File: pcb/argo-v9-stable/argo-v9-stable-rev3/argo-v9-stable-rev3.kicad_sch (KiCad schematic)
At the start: 101 parts, among them IC1 MP2672GD, J1 Sparkfun_NEO-N9M-SMA, J2 USB4125-GF-A, J3 LED_power_button_RGB_LED, J4 Conn_I2C_Molex_705450003, J5 Conn_I2C_Molex_705450003, K1 PRL3-5V-DC-1A, Q1 BSD840N, Q2 BSD840N, SW1 POW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

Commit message: **** Argo PCB rev3 sent for JLCPCB fabrication - 3d models for GPS and LORA daughterboards - improved cable connections and i2c headers - many circuit fixes to fix problems with rev2 PCB - improved overvoltage diode protection for FETs and OPi pins - fixed i2c buffer connections - improved power routing - adjusted many R values to be correct - fixed LORA pins and place LORA daughterboard on PCB - moved BNO085 to i2c connector for mounting away from power relay - many additional scope probe test points
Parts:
- added TP7: TestPoint_Probe_autonamed, Argo footprint Library:TestPoint_scope_probe_autonamed, symbol argo-v9:TestPoint_Probe_autonamed
- J1: footprint sparkfun:Sparkfun_NEO-M9N-SMA-scaled -> Argo footprint Library:Sparkfun_NEO-M9N-SMA
- J3: footprint Argo footprint Library:JST_XH_B6B-XH-AM_1x06_P2.50mm_Vertical -> Argo footprint Library:JST_XH_S6B-XH-A_1x06_P2.50mm_Horizontal
- U5: value SHT45-ADB1B -> SHT45
- U7: value TXS0102DCT -> TXS0102; specific part (none) -> TXS0102DCT
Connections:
- net 5V: now also TP7.1
- net POW_BUT: no longer J3.2 (Pin_2), POW_BUT1.2 (A), Q2.2 (G), R25.2, SW1.2, TP6.1
- new net POW_ON: J3.2 (Pin_2), POW_BUT1.2 (A), Q2.2 (G), R25.2, SW1.2, TP6.1
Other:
- note added: "3.3V zener"
- note added: "IMU BNO055 I2C addr 0x69"
- note removed: "Check !CHARGING when OPi running, might need pullup or pulldown"
- note removed: "IMU I2C addr 0x69"
- note removed: "check order!"
- moved on the sheet: D2, D3
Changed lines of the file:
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@@
 		)
 	)
-	(text "check order!"
+	(text "IMU BNO055 I2C addr 0x69"
 		(exclude_from_sim no)
-		(at 327.406 145.542 0)
-		(effects
-			(font
-				(size 1.27 1.27)
-			)
-		)
-	)
-	(text "IMU I2C addr 0x69"
-		(exclude_from_sim no)
-		(at 211.836 82.804 0)
+		(at 216.916 82.804 0)
 		(effects
 			(font
@@
 	(text "Diodes protect FET\ndrains when relay \ncoils turn off and\ncreate voltage\nspike above FUSE=battery"
 		(exclude_from_sim no)
-		(at 193.548 213.36 0)
+		(at 191.516 214.884 0)
 		(effects
 			(font
@@
 		)
 	)
+	(text "3.3V zener"
+		(exclude_from_sim no)
+		(at 214.122 209.296 0)
+		(effects
+			(font
+				(size 0.889 0.889)
+			)
+			(justify right)
+		)
+	)
 	(text "4-wire: 2 green are button,\nred/black are red LED"
 		(exclude_from_sim no)
@@
 	(text "SDP32 I2C 0x21,22,23"
 		(exclude_from_sim no)
-		(at 218.694 102.108 0)
+		(at 217.932 102.616 0)
 		(effects
 			(font
@@
 		)
 	)
-	(text "Check !CHARGING when OPi running, might need pullup or pulldown"
-		(exclude_from_sim no)
-		(at 201.168 131.318 0)
-		(effects
-			(font
-				(size 0.8382 0.8382)
-				(thickness 0.254)
-				(bold yes)
-				(color 255 0 0 1)
-			)
-		)
-	)
 	(junction
 		(at 271.78 114.3)
@@
 	)
 	(junction
-		(at 190.5 198.12)
+		(at 194.31 207.01)
 		(diameter 0)
 		(color 0 0 0 0)
@@
 	)
 	(junction
+		(at 186.69 196.85)
+		(diameter 0)
+		(color 0 0 0 0)
+	)
+	(junction
 		(at 120.65 177.8)
 		(diameter 0)
@@
 	)
 	(junction
-		(at 190.5 208.28)
-		(diameter 0)
-		(color 0 0 0 0)
-	)
-	(junction
 		(at 294.64 139.7)
 		(diameter 0)
@@
 	)
 	(junction
+		(at 176.53 179.07)
+		(diameter 0)
+		(color 0 0 0 0)
+	)
+	(junction
 		(at 224.79 201.93)
 		(diameter 0)
@@
 	(wire
 		(pts
-			(xy 185.42 208.28) (xy 190.5 208.28)
+			(xy 181.61 196.85) (xy 186.69 196.85)
 		)
 		(stroke
@@
 	(wire
 		(pts
-			(xy 224.79 196.85) (xy 224.79 201.93)
-		)
-		(stroke
-			(width 0)
-			(type default)
-		)
-	)
-	(wire
-		(pts
 			(xy 119.38 219.71) (xy 119.38 213.36)
 		)
@@
 	(wire
 		(pts
-			(xy 190.5 196.85) (xy 190.5 198.12)
+			(xy 194.31 209.55) (xy 194.31 207.01)
 		)
 		(stroke
@@
 	(wire
 		(pts
-			(xy 190.5 198.12) (xy 190.5 200.66)
+			(xy 194.31 207.01) (xy 194.31 204.47)
 		)
 		(stroke
@@
 	(wire
 		(pts
-			(xy 198.12 196.85) (xy 198.12 198.12)
+			(xy 186.69 209.55) (xy 186.69 207.01)
 		)
 		(stroke
@@
 	(wire
 		(pts
-			(xy 190.5 208.28) (xy 198.12 208.28)
+			(xy 194.31 196.85) (xy 186.69 196.85)
 		)
 		(stroke
@@
 	)
 	(label "FUSE"
-		(at 185.42 208.28 180)
+		(at 181.61 196.85 0)
 		(effects
 			(font
 				(size 1.27 1.27)
 			)
-			(justify right bottom)
+			(justify left bottom)
 		)
 	)
@@
 	)
 	(label "PSR"
-		(at 198.12 196.85 0)
+		(at 186.69 209.55 180)
 		(effects
 			(font
 				(size 1.27 1.27)
 			)
-			(justify left bottom)
+			(justify right bottom)
 		)
 	)
@@
 	)
 	(label "OFFR"
-		(at 190.5 196.85 180)
+		(at 194.31 209.55 0)
 		(effects
 			(font
 				(size 1.27 1.27)
 			)
-			(justify right bottom)
+			(justify left bottom)
 		)
 	)
@@
 			)
 		)
-		(property "Value" "TXS0102DCT"
+		(property "Value" "TXS0102"
 			(at 130.048 87.376 0)
 			(effects
@@
 			)
 		)
+		(property "specific part" "TXS0102DCT"
+			(at 135.89 82.55 0)
+			(effects
+				(font
+					(size 1.27 1.27)
+				)
+				(hide yes)
+			)
+		)
 		(pin "5"
 		)
@@
 	(symbol
 		(lib_id "argo-v9:TS4148_RCG")
-		(at 198.12 203.2 270)
+		(at 186.69 201.93 90)
 		(unit 1)
 		(exclude_from_sim no)
@@
 		(dnp no)
 		(property "Reference" "D3"
-			(at 195.58 205.74 90)
+			(at 189.23 199.39 90)
 			(effects
 				(font
@@
 		)
 		(property "Value" "TS4148_RCG"
-			(at 194.818 196.596 0)
+			(at 189.992 208.534 0)
 			(effects
 				(font
@@
 		)
 		(property "Footprint" "Argo footprint Library:DIO_TS4148_RCG"
-			(at 198.12 203.2 0)
+			(at 186.69 201.93 0)
 			(effects
 				(font
@@
 		)
 		(property "Datasheet" "https://services.ts.com.tw/storage/resources/datasheet/TS4148%20SERIES_A2301.pdf"
-			(at 198.12 203.2 0)
+			(at 186.69 201.93 0)
 			(effects
 				(font
@@
 		)
 		(property "Description" "100mA - 150mA, 75V Surface Mount Switching Diode"
-			(at 198.12 203.2 0)
+			(at 186.69 201.93 0)
 			(effects
 				(font
@@
 		)
 		(property "PARTREV" "A2301"
-			(at 198.12 203.2 0)
+			(at 186.69 201.93 0)
 			(effects
 				(font
@@
 		)
 		(property "SNAPEDA_PN" "TS4148 RCG"
-			(at 198.12 203.2 0)
+			(at 186.69 201.93 0)
 			(effects
 				(font
@@
 		)
 		(property "MANUFACTURER" "Taiwan Semiconductors"
-			(at 198.12 203.2 0)
+			(at 186.69 201.93 0)
 			(effects
 				(font
@@
 		)
 		(property "MAXIMUM_PACKAGE_HEIGHT" "0.75mm"
-			(at 198.12 203.2 0)
+			(at 186.69 201.93 0)
 			(effects
 				(font
@@
 		)
 		(property "STANDARD" "Manufacturer Recommendations"
-			(at 198.12 203.2 0)
+			(at 186.69 201.93 0)
 			(effects
 				(font
@@
 		)
 		(property "digikey" "https://www.digikey.ch/en/products/detail/taiwan-semiconductor-corporation/TS4148-RCG/7359811"
-			(at 198.12 203.2 0)
+			(at 186.69 201.93 0)
 			(effects
 				(font
@@
 			)
 		)
-		(property "Footprint" "Argo footprint Library:JST_XH_B6B-XH-AM_1x06_P2.50mm_Vertical"
+		(property "Footprint" "Argo footprint Library:JST_XH_S6B-XH-A_1x06_P2.50mm_Horizontal"
 			(at 266.7 172.466 0)
 			(effects
@@
 			)
 		)
-		(property "Footprint" "sparkfun:Sparkfun_NEO-M9N-SMA-scaled"
+		(property "Footprint" "Argo footprint Library:Sparkfun_NEO-M9N-SMA"
 			(at 187.96 59.69 0)
 			(effects
@@
 	)
 	(symbol
+		(lib_id "argo-v9:TestPoint_Probe_autonamed")
+		(at 176.53 179.07 90)
+		(unit 1)
+		(exclude_from_sim no)
+		(in_bom yes)
+		(on_board yes)
+		(dnp no)
+		(fields_autoplaced yes)
+		(property "Reference" "TP7"
+			(at 174.9425 173.99 90)
+			(effects
+				(font
+					(size 1.27 1.27)
+				)
+			)
+		)
+		(property "Value" "TestPoint_Probe_autonamed"
+			(at 172.466 177.419 0)
+			(show_name yes)
+			(effects
+				(font
+					(size 1.27 1.27)
+				)
+				(hide yes)
+			)
+		)
+		(property "Footprint" "Argo footprint Library:TestPoint_scope_probe_autonamed"
+			(at 176.53 173.99 0)
+			(effects
+				(font
+					(size 1.27 1.27)
+				)
+				(hide yes)
+			)
+		)
+		(property "Datasheet" "~"
+			(at 176.53 173.99 0)
+			(effects
+				(font
+					(size 1.27 1.27)
+				)
+				(hide yes)
+			)
+		)
+		(property "Description" "test point (alternative probe-style design)"
+			(at 176.53 179.07 0)
+			(effects
+				(font
+					(size 1.27 1.27)
+				)
+				(hide yes)
+			)
+		)
+		(pin "1"
+		)
+		(instances
+			(project ""
+				(path "/94ef8c18-8f4d-4fb8-af3c-a2b214cf3496"
+					(reference "TP7")
+					(unit 1)
+				)
+			)
+		)
+	)
+	(symbol
 		(lib_id "argo-v9:TS4148_RCG")
-		(at 190.5 203.2 270)
+		(at 194.31 201.93 90)
 		(unit 1)
 		(exclude_from_sim no)
@@
 		(dnp no)
 		(property "Reference" "D2"
-			(at 187.452 205.232 90)
+			(at 197.358 199.898 90)
 			(effects
 				(font
@@
 		)
 		(property "Value" "TS4148_RCG"
-			(at 186.436 196.596 0)
+			(at 198.374 208.534 0)
 			(effects
 				(font
@@
 		)
 		(property "Footprint" "Argo footprint Library:DIO_TS4148_RCG"
-			(at 190.5 203.2 0)
+			(at 194.31 201.93 0)
 			(effects
 				(font
@@
 		)
 		(property "Datasheet" "https://services.ts.com.tw/storage/resources/datasheet/TS4148%20SERIES_A2301.pdf"
-			(at 190.5 203.2 0)
+			(at 194.31 201.93 0)
 			(effects
 				(font
@@
 		)
 		(property "Description" "100mA - 150mA, 75V Surface Mount Switching Diode"
-			(at 190.5 203.2 0)
+			(at 194.31 201.93 0)
 			(effects
 				(font
@@
 		)
 		(property "PARTREV" "A2301"
-			(at 190.5 203.2 0)
+			(at 194.31 201.93 0)
 			(effects
 				(font
@@
 		)
 		(property "SNAPEDA_PN" "TS4148 RCG"
-			(at 190.5 203.2 0)
+			(at 194.31 201.93 0)
 			(effects
 				(font
@@
 		)
 		(property "MANUFACTURER" "Taiwan Semiconductors"
-			(at 190.5 203.2 0)
+			(at 194.31 201.93 0)
 			(effects
 				(font
@@
 		)
 		(property "MAXIMUM_PACKAGE_HEIGHT" "0.75mm"
-			(at 190.5 203.2 0)
+			(at 194.31 201.93 0)
 			(effects
 				(font
@@
 		)
 		(property "STANDARD" "Manufacturer Recommendations"
-			(at 190.5 203.2 0)
+			(at 194.31 201.93 0)
 			(effects
 				(font
@@
 		)
 		(property "digikey" "https://www.digikey.ch/en/products/detail/taiwan-semiconductor-corporation/TS4148-RCG/7359811"
-			(at 190.5 203.2 0)
+			(at 194.31 201.93 0)
 			(effects
 				(font
@@
 			)
 		)
-		(property "Value" "SHT45-ADB1B"
+		(property "Value" "SHT45"
 			(at 242.57 138.4299 0)
 			(effects

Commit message: argo pcb updates after fab to make things better like visible silkscreen and componet imperovmeents
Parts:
- J4, J5: digikey (150um finish) (none) -> https://www.digikey.ch/en/products/detail/molex/0705450003/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; farnell (none) -> https://ch.farnell.com/molex/70545-0003/connector-header-4p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; series (none) -> https://www.molex.com/en-us/products/series-chart/70545
- R26, R27, R28, R29, R30, R31, R32, R7B1: now not fitted
- TP1, TP10, TP11, TP2, TP3, TP4, TP5, TP6, TP7, TP8, TP9: now left out of the parts list
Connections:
- net ISET: now reaches IC1.5 (ISET), R11.2
- net NTC: now reaches IC1.8 (NTC), R13.2, R21.1
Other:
- note added: "!PG configure as PU - signals that CH221K has found a PD cable (power delivery) and negociated the 5V VBUS. But failure also just indicates original USB (non PD) cable."
- note removed: "!PG configure as PU - signals USB power"
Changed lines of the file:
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@@
 		)
 	)
-	(text "!PG configure as PU - signals USB power"
+	(text "!PG configure as PU - signals that CH221K has found \na PD cable (power delivery) and negociated the 5V VBUS.\nBut failure also just indicates original USB (non PD) cable."
 		(exclude_from_sim no)
 		(at 169.418 136.144 0)
 		(effects
 			(font
-				(size 1.016 1.016)
+				(size 0.762 0.762)
 			)
 			(justify left)
@@
 		)
 	)
+	(label "ISET"
+		(at 290.83 110.49 0)
+		(effects
+			(font
+				(size 1.27 1.27)
+			)
+			(justify left bottom)
+		)
+	)
 	(label "BAT_MID"
 		(at 318.77 139.7 0)
@@
 		)
 	)
+	(label "NTC"
+		(at 288.29 118.11 0)
+		(effects
+			(font
+				(size 1.27 1.27)
+			)
+			(justify left bottom)
+		)
+	)
 	(label "!PG"
 		(at 382.27 181.61 0)
@@
 		(in_bom yes)
 		(on_board yes)
-		(dnp no)
+		(dnp yes)
 		(property "Reference" "R30"
 			(at 342.392 116.332 90)
@@
 		(unit 1)
 		(exclude_from_sim no)
-		(in_bom yes)
+		(in_bom no)
 		(on_board yes)
 		(dnp no)
@@
 		(in_bom yes)
 		(on_board yes)
-		(dnp no)
+		(dnp yes)
 		(property "Reference" "R28"
 			(at 113.284 85.852 90)
@@
 		(unit 1)
 		(exclude_from_sim no)
-		(in_bom yes)
+		(in_bom no)
 		(on_board yes)
 		(dnp no)
@@
 			)
 		)
-		(property "Datasheet" "https://www.wch.cn/downloads/file/301.html"
+		(property "Datasheet" "kicad-embed://CH224DS1.PDF"
 			(at 372.11 165.1 0)
 			(effects
@@
 		(in_bom yes)
 		(on_board yes)
-		(dnp no)
+		(dnp yes)
 		(property "Reference" "R29"
 			(at 111.252 76.962 90)
@@
 		(unit 1)
 		(exclude_from_sim no)
-		(in_bom yes)
+		(in_bom no)
 		(on_board yes)
 		(dnp no)
@@
 		(unit 1)
 		(exclude_from_sim no)
-		(in_bom yes)
+		(in_bom no)
 		(on_board yes)
 		(dnp no)
@@
 		(in_bom yes)
 		(on_board yes)
-		(dnp no)
+		(dnp yes)
 		(property "Reference" "R7B1"
 			(at 114.808 180.34 0)
@@
 		(in_bom yes)
 		(on_board yes)
-		(dnp no)
+		(dnp yes)
 		(property "Reference" "R27"
 			(at 105.918 90.678 90)
@@
 			)
 		)
+		(property "series" "https://www.molex.com/en-us/products/series-chart/70545"
+			(at 214.63 74.93 0)
+			(effects
+				(font
+					(size 1.27 1.27)
+				)
+				(hide yes)
+			)
+		)
+		(property "farnell" "https://ch.farnell.com/molex/70545-0003/connector-header-4pos-1row-2-54mm/dp/3221916"
+			(at 214.63 74.93 0)
+			(effects
+				(font
+					(size 1.27 1.27)
+				)
+				(hide yes)
+			)
+		)
+		(property "digikey (150um finish)" "https://www.digikey.ch/en/products/detail/molex/0705450003/455677?s=N4IgjCBcoBw1oDGUBmBDANgZwKYBoQB7KAbRACYAGAZjADYB2EAXQIAcAXKEAZQ4CcAlgDsA5iAC%2BBMAwCc5BCGSR02fEVIhZsgKx0IrEJ258hYyQQC0AFkXLVuAgDdhqTI42QyO6w3ot2LkgQSQkJIA"
+			(at 214.63 74.93 0)
+			(effects
+				(font
+					(size 1.27 1.27)
+				)
+				(hide yes)
+			)
+		)
 		(pin "2"
 		)
@@
 		(unit 1)
 		(exclude_from_sim no)
-		(in_bom yes)
+		(in_bom no)
 		(on_board yes)
 		(dnp no)
@@
 			)
 		)
+		(property "series" "https://www.molex.com/en-us/products/series-chart/70545"
+			(at 214.63 93.98 0)
+			(effects
+				(font
+					(size 1.27 1.27)
+				)
+				(hide yes)
+			)
+		)
+		(property "farnell" "https://ch.farnell.com/molex/70545-0003/connector-header-4pos-1row-2-54mm/dp/3221916"
+			(at 214.63 93.98 0)
+			(effects
+				(font
+					(size 1.27 1.27)
+				)
+				(hide yes)
+			)
+		)
+		(property "digikey (150um finish)" "https://www.digikey.ch/en/products/detail/molex/0705450003/455677?s=N4IgjCBcoBw1oDGUBmBDANgZwKYBoQB7KAbRACYAGAZjADYB2EAXQIAcAXKEAZQ4CcAlgDsA5iAC%2BBMAwCc5BCGSR02fEVIhZsgKx0IrEJ258hYyQQC0AFkXLVuAgDdhqTI42QyO6w3ot2LkgQSQkJIA"
+			(at 214.63 93.98 0)
+			(effects
+				(font
+					(size 1.27 1.27)
+				)
+				(hide yes)
+			)
+		)
 		(pin "2"
 		)
@@
 		(unit 1)
 		(exclude_from_sim no)
-		(in_bom yes)
+		(in_bom no)
 		(on_board yes)
 		(dnp no)
@@
 		(in_bom yes)
 		(on_board yes)
-		(dnp no)
+		(dnp yes)
 		(property "Reference" "R32"
 			(at 341.884 105.41 90)
@@
 		(unit 1)
 		(exclude_from_sim no)
-		(in_bom yes)
+		(in_bom no)
 		(on_board yes)
 		(dnp no)
@@
 		(unit 1)
 		(exclude_from_sim no)
-		(in_bom yes)
+		(in_bom no)
 		(on_board yes)
 		(dnp no)
@@
 		(unit 1)
 		(exclude_from_sim no)
-		(in_bom yes)
+		(in_bom no)
 		(on_board yes)
 		(dnp no)
@@
 		(unit 1)
 		(exclude_from_sim no)
-		(in_bom yes)
+		(in_bom no)
 		(on_board yes)
 		(dnp no)
@@
 		(in_bom yes)
 		(on_board yes)
-		(dnp no)
+		(dnp yes)
 		(property "Reference" "R26"
 			(at 107.188 81.534 90)
@@
 		(unit 1)
 		(exclude_from_sim no)
-		(in_bom yes)
+		(in_bom no)
 		(on_board yes)
 		(dnp no)
@@
 		(in_bom yes)
 		(on_board yes)
-		(dnp no)
+		(dnp yes)
 		(property "Reference" "R31"
 			(at 342.646 119.38 90)

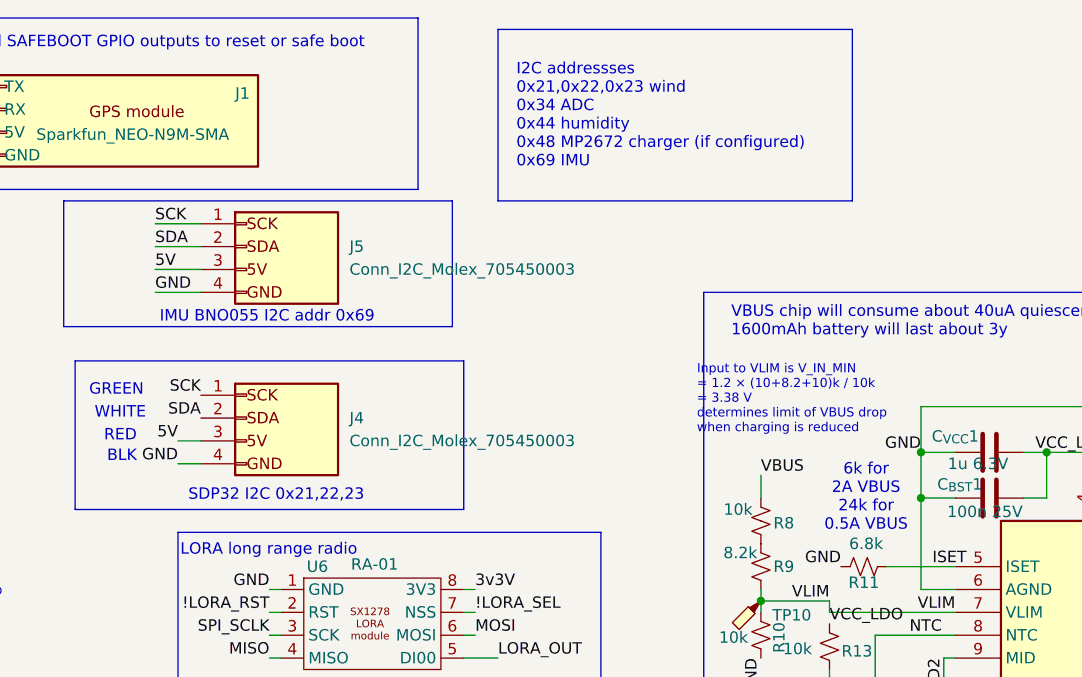
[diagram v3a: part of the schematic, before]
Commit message: add LP5814DLR I2C address 0x2C
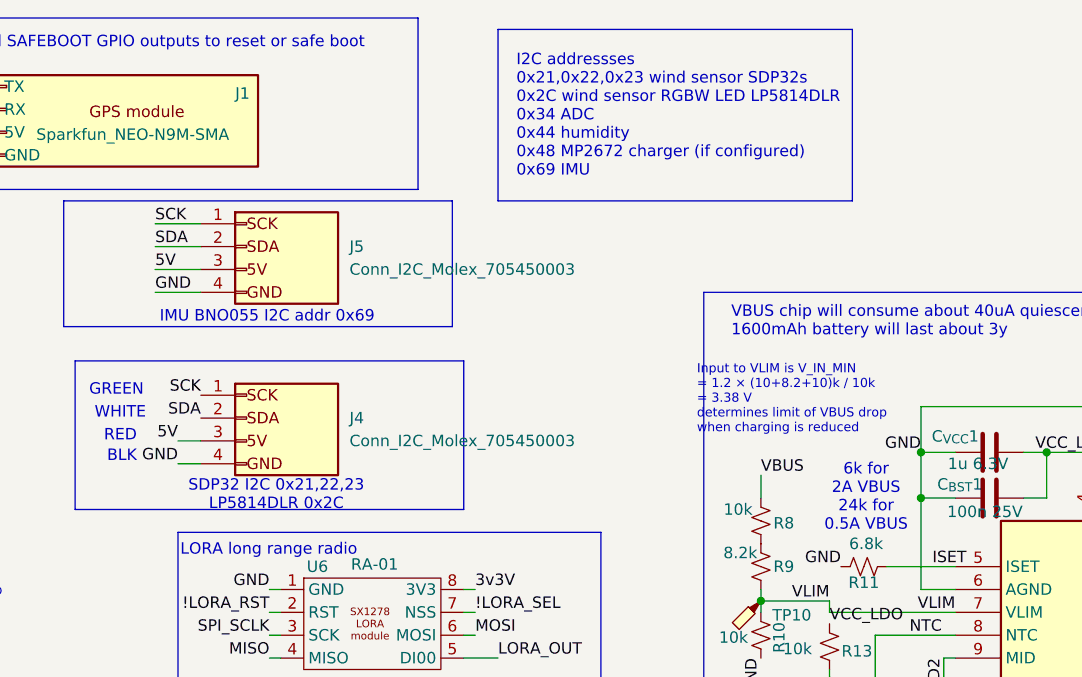
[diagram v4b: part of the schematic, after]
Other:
- note added: "I2C addressses 0x21,0x22,0x23 wind sensor SDP32s 0x2C wind sensor RGBW LED LP5814DLR 0x34 ADC 0x44 humidity 0x48 MP2672 charger (if configured) 0x69 IMU"
- note added: "SDP32 I2C 0x21,22,23 LP5814DLR 0x2C"
- note removed: "I2C addressses 0x21,0x22,0x23 wind 0x34 ADC 0x44 humidity 0x48 MP2672 charger (if configured) 0x69 IMU"
- note removed: "SDP32 I2C 0x21,22,23"
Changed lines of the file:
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@@
 		)
 	)
-	(text "I2C addressses\n0x21,0x22,0x23 wind\n0x34 ADC\n0x44 humidity\n0x48 MP2672 charger (if configured)\n0x69 IMU"
+	(text "I2C addressses\n0x21,0x22,0x23 wind sensor SDP32s\n0x2C wind sensor RGBW LED LP5814DLR\n0x34 ADC\n0x44 humidity\n0x48 MP2672 charger (if configured)\n0x69 IMU"
 		(exclude_from_sim no)
 		(at 244.602 60.452 0)
@@
 		)
 	)
-	(text "SDP32 I2C 0x21,22,23"
+	(text "SDP32 I2C 0x21,22,23\nLP5814DLR 0x2C"
 		(exclude_from_sim no)
 		(at 217.932 102.616 0)
